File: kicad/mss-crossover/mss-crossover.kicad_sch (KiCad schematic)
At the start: 36 parts, among them J1 Screw_Terminal_01x02, J2 AVR-ISP, J3 8P8C, J4 8P8C, SW1 FSM4JSMATR, T1 PE-51687, U1 AP7381-33Y, U2 INA180A4, U3 ATtiny85-20S, U4 TLP241A

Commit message: Initial PCB layout complete on v2.0
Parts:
- removed D10: SMAJ18A-TP, Diode_SMD:D_SMA, symbol Diode:SM6T75A
- added C6: 0.1uF, Capacitor_SMD:C_0805_2012Metric, symbol Device:C
- SW1: footprint digikey-footprints:Switch_Tactile_SMD_6x6mm -> ISE_Generic:TE_FSM4JSMA
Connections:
- net +3.3V: now also C6.2
- net GND: now also D7.1 (K), D8.1 (K), U4.2; no longer R2.2, R3.2, R6.2
- net /CAL_SW: now reaches C4.1, SW1.1, SW1.2, U3.2 (XTAL1/PB3)
- net at J2.4 (MOSI), U3.5 (AREF/PB0): now also R3.1; no longer D8.2 (A)
- net at J2.1 (MISO), U3.6 (PB1): now also R2.1, R6.2; no longer D7.2 (A), U4.1
- net at D5.1 (K), D5.2 (A), R4.2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: now also C6.1
- net at R6.1: now also U4.1; no longer U4.2
- new net: D8.2 (A), R3.2
- new net: D7.2 (A), R2.2
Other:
- moved on the sheet: D5, D7, D8, R2, R3, R4

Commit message: Updates per review
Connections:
- net /CAL_SW renamed ~{CAL_SW}

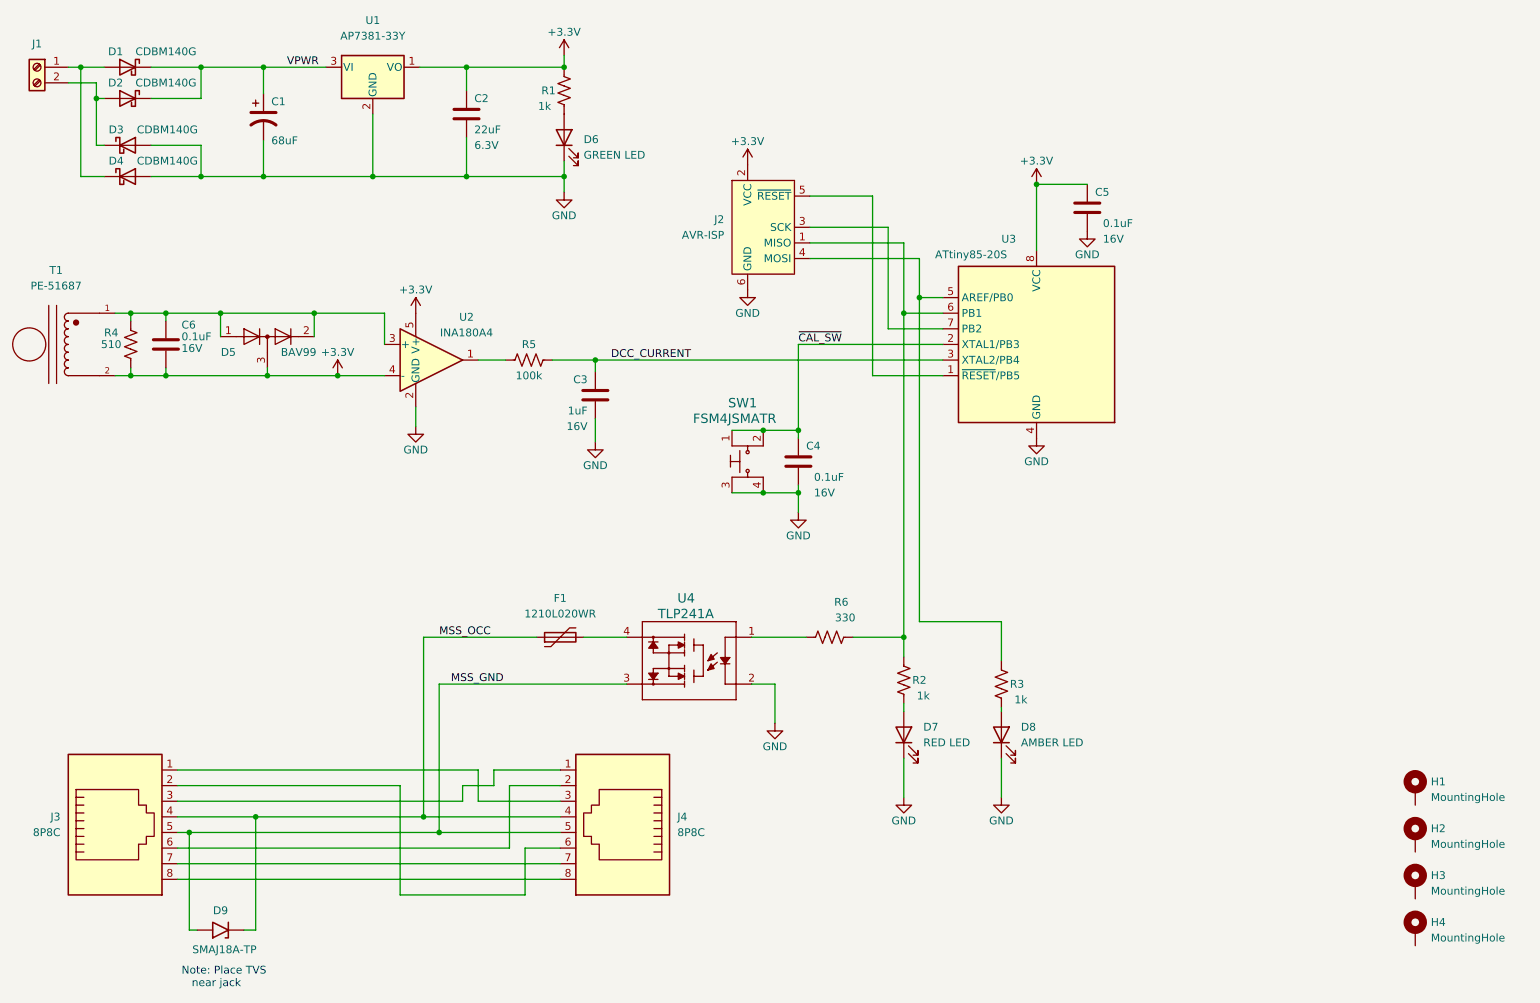
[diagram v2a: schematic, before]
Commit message: Add test points
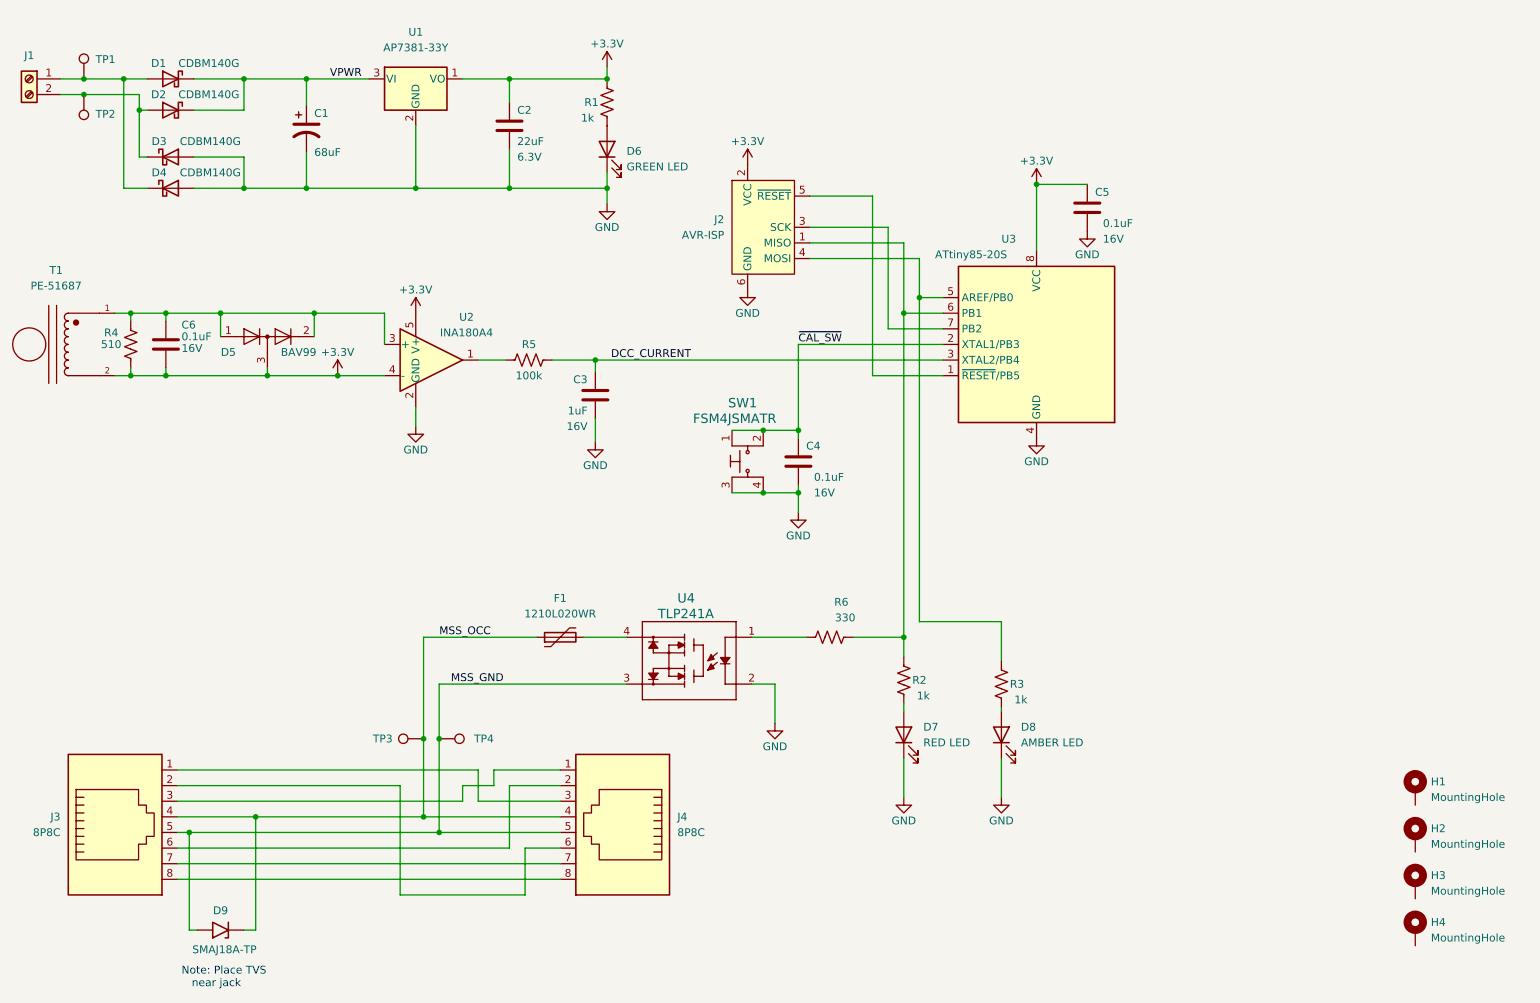
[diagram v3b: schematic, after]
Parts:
- added TP1, TP2, TP3, TP4: TestPoint, TestPoint:TestPoint_Pad_D2.0mm, symbol Connector:TestPoint
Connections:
- net MSS_GND: now also TP4.1
- net MSS_OCC: now also TP3.1
- net at D1.2 (A), D4.1 (K), J1.1 (Pin_1): now also TP1.1
- net at D2.2 (A), D3.1 (K), J1.2 (Pin_2): now also TP2.1
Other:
- moved on the sheet: C1, C2, D1, D2, D3, D4, D6, J1, R1, U1

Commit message: Update schematic footprints from PCB changes
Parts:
- D1, D2, D3, D4: footprint Diode_SMD:D_SOD-123 -> ISE_Generic:SOD-123T
- J3, J4: footprint RJ45_Amphenol_54602-x08_Horizontal -> Connector_RJ:RJ45_Amphenol_54602-x08_Horizontal
- U3: footprint Package_SO:SOIC-8W_5.3x5.3mm_P1.27mm -> ISE_Generic:ATMEL_SO8_DUAL

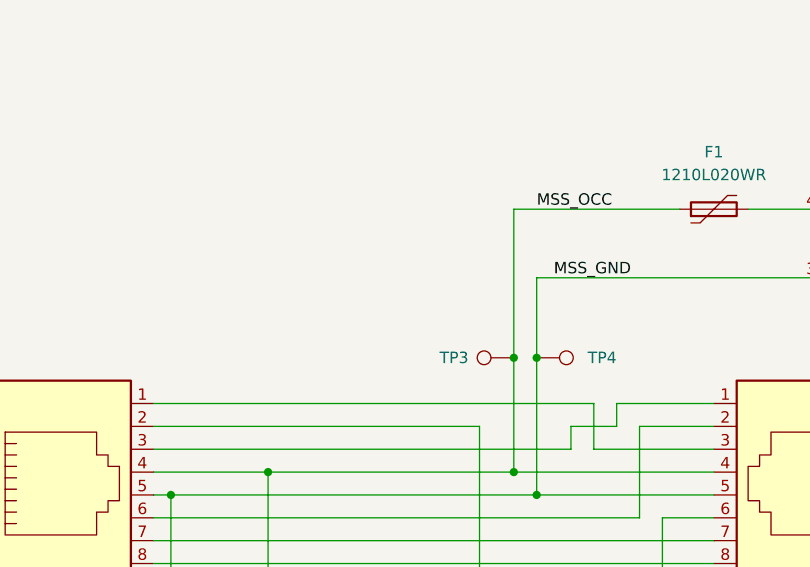
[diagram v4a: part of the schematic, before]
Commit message: Add auxilliary detection terminal block
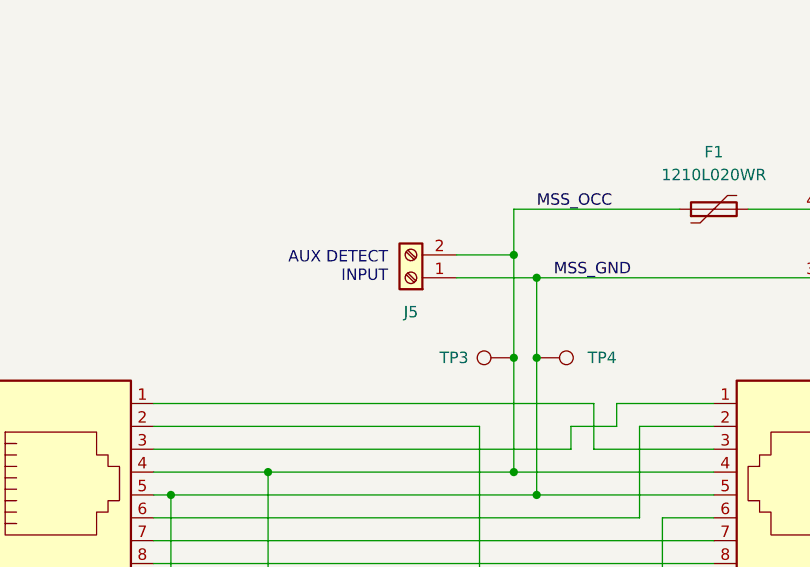
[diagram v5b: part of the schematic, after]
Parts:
- added J5: Screw_Terminal_01x02, TerminalBlock_RND:TerminalBlock_RND_205-00012_1x02_P5.00mm_Horizontal, symbol Connector:Screw_Terminal_01x02
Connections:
- net MSS_GND: now also J5.1 (Pin_1)
- net MSS_OCC: now also J5.2 (Pin_2)
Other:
- note added: "AUX DETECT INPUT"
